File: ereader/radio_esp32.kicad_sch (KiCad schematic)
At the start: 32 parts, among them U25 TXU0102DCUR, U3 ESP32-C6-WROOM-1-N8, U4 TPS22964CYZPT, U5 TXU0304PWR, U6 TPS389001DSET, U7 SN74LVC1G97DBVR, U8 SN74LVC1G97DBVR

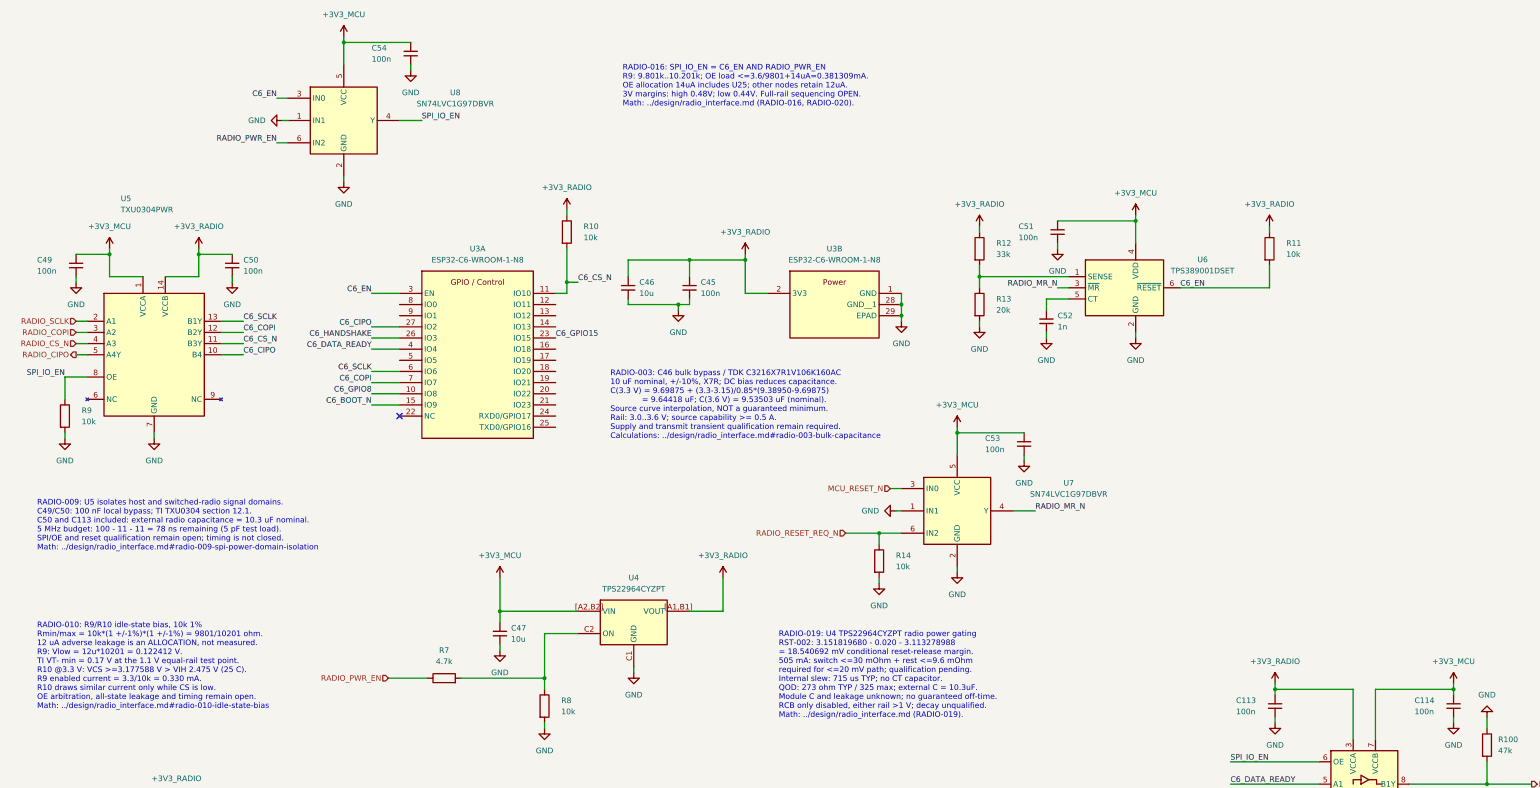
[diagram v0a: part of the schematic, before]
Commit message: WIP: integrate orientation sensor and refresh schematic review exports
Add LIS2DW12 host wiring and sourced passives, revise held-supply discharge calculations, document camera and capacitance screens, and refresh standard capacitor caches. Include reviewed 14-page PDF and reconciled native BOM. ERC remains 111 errors and 11 warnings; electrical design is incomplete. Refs #21.
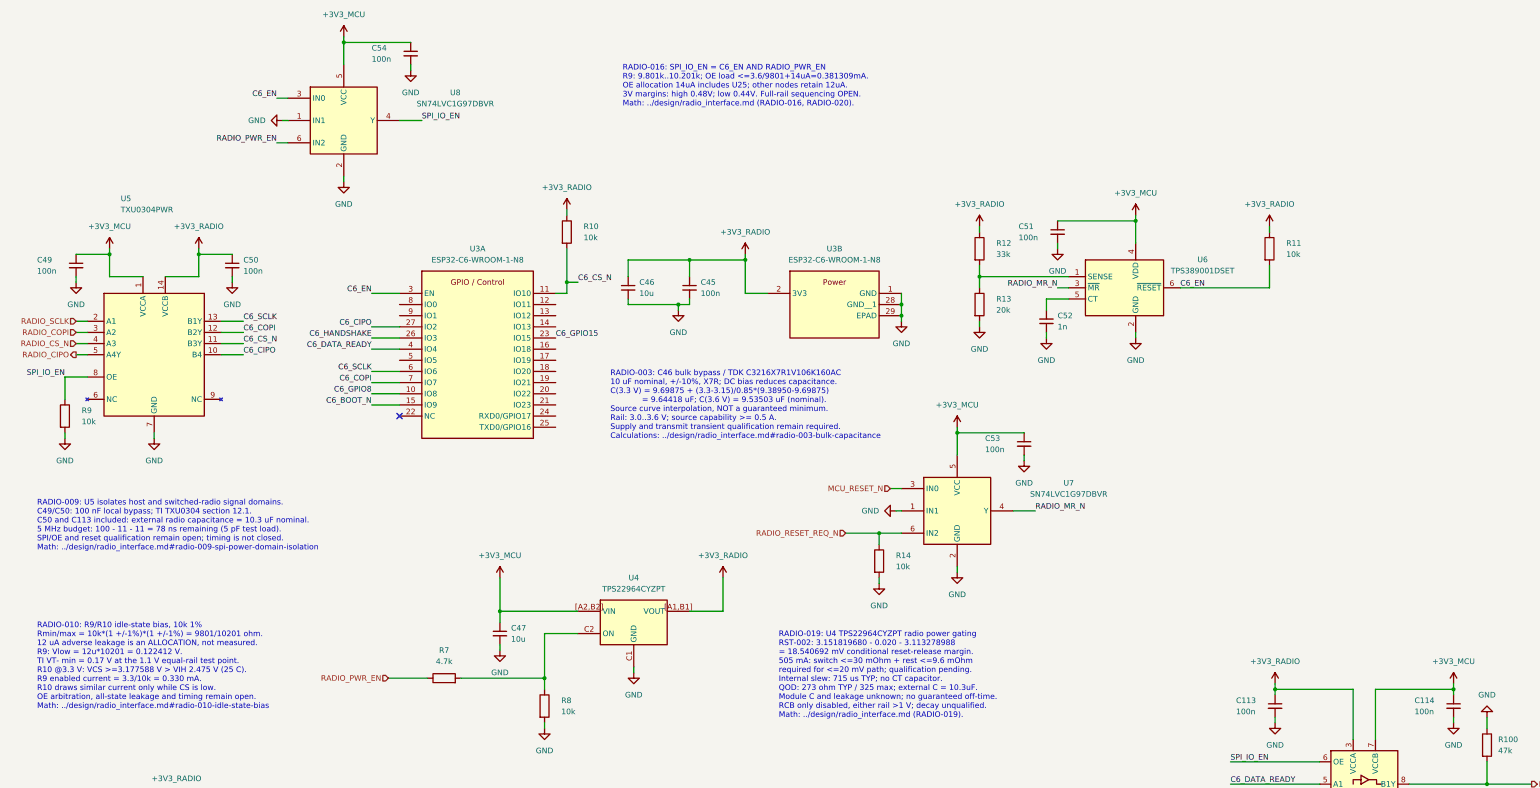
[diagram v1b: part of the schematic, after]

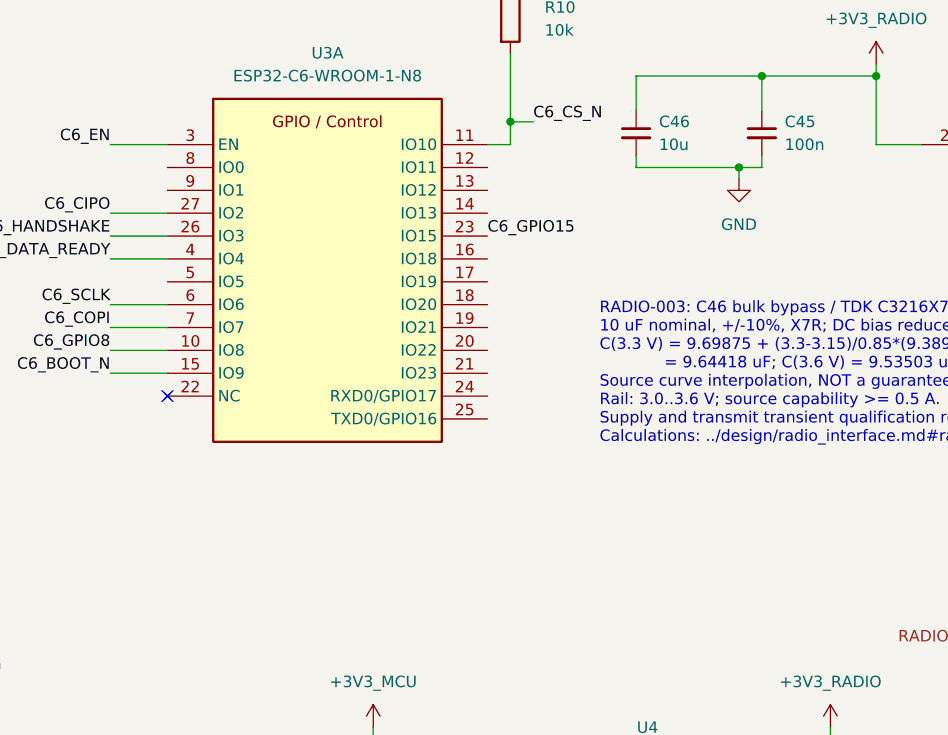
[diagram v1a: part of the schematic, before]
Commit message: Document and mark unused radio GPIOs while preserving recovery pins
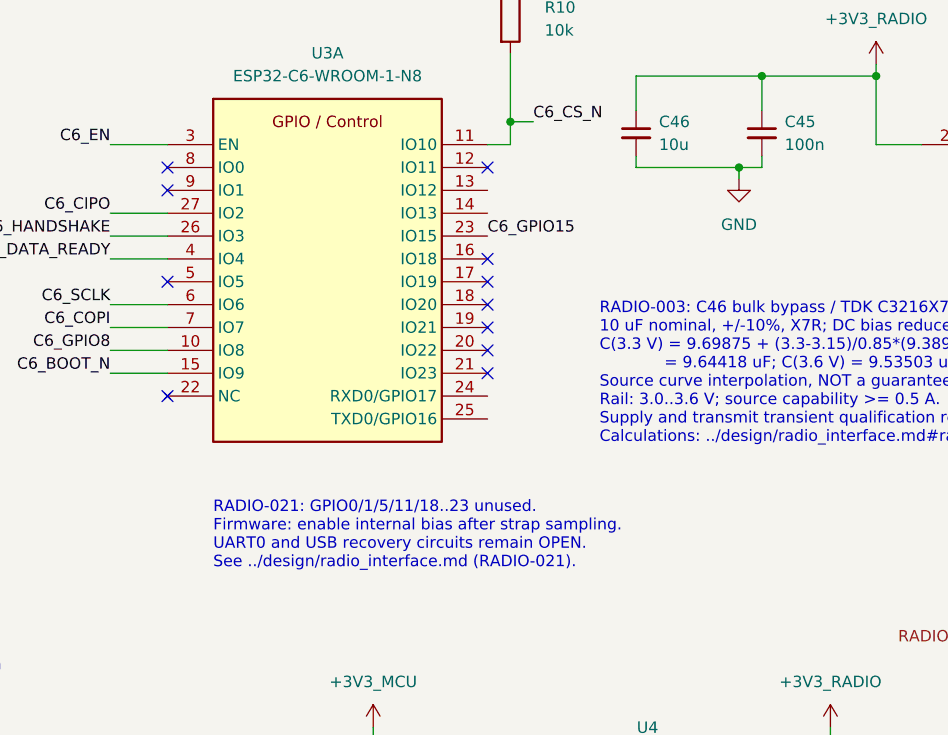
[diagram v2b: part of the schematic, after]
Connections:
- no-connect marks 1 -> 11
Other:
- note added: "RADIO-021: GPIO0/1/5/11/18..23 unused. Firmware: enable internal bias after strap sampling. UART0 and USB recovery circuits remain OPEN. See ../design/radio_interface.md (RADIO-021)."
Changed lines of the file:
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@@
+		)
+	)
+	(text "RADIO-021: GPIO0/1/5/11/18..23 unused.\nFirmware: enable internal bias after strap sampling.\nUART0 and USB recovery circuits remain OPEN.\nSee ../design/radio_interface.md (RADIO-021)."
+		(exclude_from_sim no)
+		(at 106.68 120.904 0)
+		(effects
+			(font
+				(size 1.27 1.27)
+			)
+			(justify left)
 		)
 	)
@@
 	)
 	(no_connect
+		(at 137.16 100.33)
+	)
+	(no_connect
+		(at 137.16 102.87)
+	)
+	(no_connect
+		(at 101.6 82.55)
+	)
+	(no_connect
+		(at 137.16 90.17)
+	)
+	(no_connect
+		(at 101.6 80.01)
+	)
+	(no_connect
+		(at 137.16 80.01)
+	)
+	(no_connect
+		(at 137.16 95.25)
+	)
+	(no_connect
 		(at 101.6 105.41)
 	)
+	(no_connect
+		(at 137.16 92.71)
+	)
+	(no_connect
+		(at 101.6 92.71)
+	)
+	(no_connect
+		(at 137.16 97.79)
+	)
 	(wire

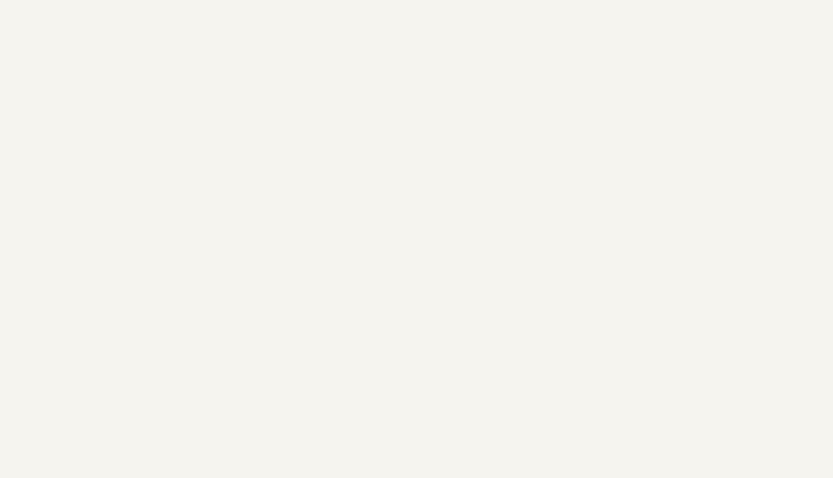
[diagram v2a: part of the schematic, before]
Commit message: Checkpoint native UART translator placement and refresh schematic PDF
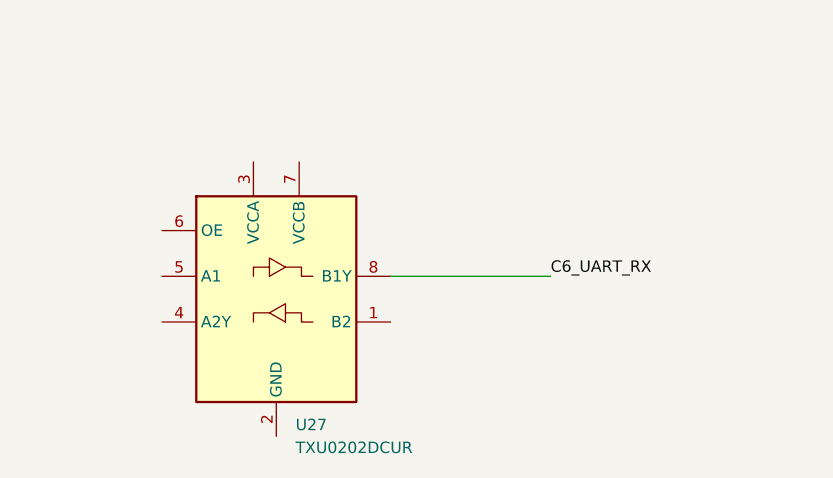
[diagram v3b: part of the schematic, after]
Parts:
- added U27: TXU0202DCUR, symbol Power_Devices:TXU0202DCUR
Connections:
- new net C6_UART_RX: U27.8 (B1Y)
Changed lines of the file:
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@@
 	(wire
 		(pts
+			(xy 160.02 328.93) (xy 177.8 328.93)
+		)
+		(stroke
+			(width 0)
+			(type default)
+		)
+	)
+	(wire
+		(pts
 			(xy 139.7 74.93) (xy 139.7 77.47)
 		)
@@
 		)
 	)
+	(label "C6_UART_RX"
+		(at 177.8 328.93 0)
+		(effects
+			(font
+				(size 1.27 1.27)
+			)
+			(justify left bottom)
+		)
+	)
 	(label "C6_HANDSHAKE"
 		(at 95.25 87.63 180)
@@
 					(unit 1)
 				)
+			)
+		)
+	)
+	(symbol
+		(lib_id "Power_Devices:TXU0202DCUR")
+		(at 147.32 331.47 0)
+		(unit 1)
+		(body_style 1)
+		(exclude_from_sim no)
+		(in_bom yes)
+		(on_board yes)
+		(in_pos_files yes)
+		(dnp no)
+		(fields_autoplaced yes)
+		(property "Reference" "U27"
+			(at 149.4633 345.44 0)
+			(show_name no)
+			(do_not_autoplace no)
+			(effects
+				(font
+					(size 1.27 1.27)
+				)
+				(justify left)
+			)
+		)
+		(property "Value" "TXU0202DCUR"
+			(at 149.4633 347.98 0)
+			(show_name no)
+			(do_not_autoplace no)
+			(effects
+				(font
+					(size 1.27 1.27)
+				)
+				(justify left)
+			)
+		)
+		(property "Footprint" ""
+			(at 147.32 345.44 0)
+			(hide yes)
+			(show_name no)
+			(do_not_autoplace no)
+			(effects
+				(font
+					(size 1.27 1.27)
+				)
+			)
+		)
+		(property "Datasheet" "https://www.ti.com/lit/ds/symlink/txu0202.pdf"
+			(at 147.32 332.232 0)
+			(hide yes)
+			(show_name no)
+			(do_not_autoplace no)
+			(effects
+				(font
+					(size 1.27 1.27)
+				)
+			)
+		)
+		(property "Description" "TI TXU0202DCUR; one A-to-B and one B-to-A fixed-direction translator, active-high OE, 1.1..5.5 V, VSSOP-8 DCU. Pins 1=B2, 2=GND, 3=VCCA, 4=A2Y, 5=A1, 6=OE, 7=VCCB, 8=B1Y. SCES942A Table 6-1."
+			(at 147.32 331.47 0)
+			(hide yes)
+			(show_name no)
+			(do_not_autoplace no)
+			(effects
+				(font
+					(size 1.27 1.27)
+				)
+			)
+		)
+		(property "Manufacturer_Name" "Texas Instruments"
+			(at 147.32 331.47 0)
+			(hide yes)
+			(show_name no)
+			(do_not_autoplace no)
+			(effects
+				(font
+					(size 1.27 1.27)
+				)
+			)
+		)
+		(property "Manufacturer_Part_Number" "TXU0202DCUR"
+			(at 147.32 331.47 0)
+			(hide yes)
+			(show_name no)
+			(do_not_autoplace no)
+			(effects
+				(font
+					(size 1.27 1.27)
+				)
+			)
+		)
+		(property "DigiKey_Part_Number" "296-TXU0202DCURCT-ND"
+			(at 147.32 331.47 0)
+			(hide yes)
+			(show_name no)
+			(do_not_autoplace no)
+			(effects
+				(font
+					(size 1.27 1.27)
+				)
+			)
+		)
+		(property "DigiKey_URL" "https://www.digikey.com/en/products/detail/texas-instruments/TXU0202DCUR/16677096"
+			(at 147.32 331.47 0)
+			(hide yes)
+			(show_name no)
+			(do_not_autoplace no)
+			(effects
+				(font
+					(size 1.27 1.27)
+				)
+			)
+		)
+		(pin "2"
+		)
+		(pin "4"
+		)
+		(pin "6"
+		)
+		(pin "3"
+		)
+		(pin "1"
+		)
+		(pin "5"
+		)
+		(pin "8"
+		)
+		(pin "7"
+		)
+		(instances
+			(project "ereader_rev1"
+				(path "/0586cc51-9c57-495b-a0c9-c29ba0d48166/9b84c337-6879-4714-899e-3993bcc30b88"
+					(reference "U27")
+					(unit 1)
+				)

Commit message: Wire radio service UART and ground; refresh schematic PDF
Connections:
- net C6_UART_RX: now also U3.24 (RXD0/GPIO17)
- net GND: now also U27.2 (GND)
- net C6_UART_TX: now reaches U3.25 (TXD0/GPIO16)
- net C6_UART_TX: now also U27.1 (B2)
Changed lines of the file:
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@@
 	(wire
 		(pts
+			(xy 137.16 107.95) (xy 139.7 107.95)
+		)
+		(stroke
+			(width 0)
+			(type default)
+		)
+	)
+	(wire
+		(pts
 			(xy 233.68 62.23) (xy 233.68 63.5)
 		)
@@
 	(wire
 		(pts
+			(xy 142.24 105.41) (xy 142.24 113.03)
+		)
+		(stroke
+			(width 0)
+			(type default)
+		)
+	)
+	(wire
+		(pts
 			(xy 124.46 158.75) (xy 124.46 157.48)
 		)
@@
 	(wire
 		(pts
+			(xy 147.32 346.71) (xy 147.32 351.79)
+		)
+		(stroke
+			(width 0)
+			(type default)
+		)
+	)
+	(wire
+		(pts
 			(xy 243.84 109.22) (xy 228.6 109.22)
 		)
@@
 	(wire
 		(pts
+			(xy 137.16 105.41) (xy 142.24 105.41)
+		)
+		(stroke
+			(width 0)
+			(type default)
+		)
+	)
+	(wire
+		(pts
 			(xy 95.25 100.33) (xy 101.6 100.33)
 		)
@@
 	(wire
 		(pts
+			(xy 160.02 334.01) (xy 177.8 334.01)
+		)
+		(stroke
+			(width 0)
+			(type default)
+		)
+	)
+	(wire
+		(pts
 			(xy 60.96 91.44) (xy 66.04 91.44)
 		)
@@
 	(wire
 		(pts
+			(xy 139.7 107.95) (xy 139.7 115.57)
+		)
+		(stroke
+			(width 0)
+			(type default)
+		)
+	)
+	(wire
+		(pts
 			(xy 25.4 193.04) (xy 25.4 199.39)
 		)
@@
 		)
 	)
+	(label "C6_UART_TX"
+		(at 177.8 334.01 0)
+		(effects
+			(font
+				(size 1.27 1.27)
+			)
+			(justify left bottom)
+		)
+	)
 	(label "C6_DATA_READY"
 		(at 290.83 189.23 0)
@@
 		)
 	)
+	(label "C6_UART_RX"
+		(at 142.24 113.03 0)
+		(effects
+			(font
+				(size 1.27 1.27)
+			)
+			(justify left bottom)
+		)
+	)
 	(label "C6_COPI"
 		(at 66.04 86.36 0)
@@
 		)
 	)
+	(label "C6_UART_TX"
+		(at 139.7 115.57 0)
+		(effects
+			(font
+				(size 1.27 1.27)
+			)
+			(justify left bottom)
+		)
+	)
 	(label "C6_SCLK"
 		(at 66.04 83.82 0)
@@
 					(unit 1)
 				)
+			)
+		)
+	)
+	(symbol
+		(lib_id "power:GND")
+		(at 147.32 351.79 0)
+		(unit 1)
+		(body_style 1)
+		(exclude_from_sim no)
+		(in_bom yes)
+		(on_board yes)
+		(in_pos_files yes)
+		(dnp no)
+		(fields_autoplaced yes)
+		(property "Reference" "#PWR0241"
+			(at 147.32 358.14 0)
+			(hide yes)
+			(show_name no)
+			(do_not_autoplace no)
+			(effects
+				(font
+					(size 1.27 1.27)
+				)
+			)
+		)
+		(property "Value" "GND"
+			(at 147.32 356.87 0)
+			(show_name no)
+			(do_not_autoplace no)
+			(effects
+				(font
+					(size 1.27 1.27)
+				)
+			)
+		)
+		(property "Footprint" ""
+			(at 147.32 351.79 0)
+			(hide yes)
+			(show_name no)
+			(do_not_autoplace no)
+			(effects
+				(font
+					(size 1.27 1.27)
+				)
+			)
+		)
+		(property "Datasheet" ""
+			(at 147.32 351.79 0)
+			(hide yes)
+			(show_name no)
+			(do_not_autoplace no)
+			(effects
+				(font
+					(size 1.27 1.27)
+				)
+			)
+		)
+		(property "Description" "Power symbol creates a global label with name \"GND\" , ground"
+			(at 147.32 351.79 0)
+			(hide yes)
+			(show_name no)
+			(do_not_autoplace no)
+			(effects
+				(font
+					(size 1.27 1.27)
+				)
+			)
+		)
+		(pin "1"
+		)
+		(instances
+			(project "ereader_rev1"
+				(path "/0586cc51-9c57-495b-a0c9-c29ba0d48166/9b84c337-6879-4714-899e-3993bcc30b88"
+					(reference "#PWR0241")
+					(unit 1)
+				)

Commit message: Route isolated UART supply domains and refresh schematic PDF
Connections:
- net +3V3_RADIO: now also U27.7 (VCCB)
- net SERVICE_VIO: now reaches U27.3 (VCCA)
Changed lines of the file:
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@@
 	(wire
 		(pts
+			(xy 124.46 306.07) (xy 144.78 306.07)
+		)
+		(stroke
+			(width 0)
+			(type default)
+		)
+	)
+	(wire
+		(pts
 			(xy 185.42 77.47) (xy 180.34 77.47)
 		)
@@
 	(wire
 		(pts
+			(xy 149.86 306.07) (xy 170.18 306.07)
+		)
+		(stroke
+			(width 0)
+			(type default)
+		)
+	)
+	(wire
+		(pts
 			(xy 299.72 62.23) (xy 299.72 63.5)
 		)
@@
 	(wire
 		(pts
+			(xy 149.86 316.23) (xy 149.86 306.07)
+		)
+		(stroke
+			(width 0)
+			(type default)
+		)
+	)
+	(wire
+		(pts
 			(xy 60.96 86.36) (xy 66.04 86.36)
 		)
@@
 	(wire
 		(pts
+			(xy 144.78 316.23) (xy 144.78 306.07)
+		)
+		(stroke
+			(width 0)
+			(type default)
+		)
+	)
+	(wire
+		(pts
 			(xy 73.66 43.18) (xy 76.2 43.18)
 		)
@@
 		)
 	)
+	(label "SERVICE_VIO"
+		(at 124.46 306.07 0)
+		(effects
+			(font
+				(size 1.27 1.27)
+			)
+			(justify left bottom)
+		)
+	)
 	(label "C6_EN"
 		(at 73.66 33.02 180)
@@
 					(unit 1)
 				)
+			)
+		)
+	)
+	(symbol
+		(lib_id "power:+3V3")
+		(at 170.18 306.07 0)
+		(unit 1)
+		(body_style 1)
+		(exclude_from_sim no)
+		(in_bom yes)
+		(on_board yes)
+		(in_pos_files yes)
+		(dnp no)
+		(fields_autoplaced yes)
+		(property "Reference" "#PWR0242"
+			(at 170.18 309.88 0)
+			(hide yes)
+			(show_name no)
+			(do_not_autoplace no)
+			(effects
+				(font
+					(size 1.27 1.27)
+				)
+			)
+		)
+		(property "Value" "+3V3_RADIO"
+			(at 170.18 300.99 0)
+			(show_name no)
+			(do_not_autoplace no)
+			(effects
+				(font
+					(size 1.27 1.27)
+				)
+			)
+		)
+		(property "Footprint" ""
+			(at 170.18 306.07 0)
+			(hide yes)
+			(show_name no)
+			(do_not_autoplace no)
+			(effects
+				(font
+					(size 1.27 1.27)
+				)
+			)
+		)
+		(property "Datasheet" ""
+			(at 170.18 306.07 0)
+			(hide yes)
+			(show_name no)
+			(do_not_autoplace no)
+			(effects
+				(font
+					(size 1.27 1.27)
+				)
+			)
+		)
+		(property "Description" "Power symbol creates a global label with name \"+3V3\""
+			(at 170.18 306.07 0)
+			(hide yes)
+			(show_name no)
+			(do_not_autoplace no)
+			(effects
+				(font
+					(size 1.27 1.27)
+				)
+			)
+		)
+		(pin "1"
+		)
+		(instances
+			(project "ereader_rev1"
+				(path "/0586cc51-9c57-495b-a0c9-c29ba0d48166/9b84c337-6879-4714-899e-3993bcc30b88"
+					(reference "#PWR0242")
+					(unit 1)
+				)

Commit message: Add service UART supply bypass capacitors and refresh PDF
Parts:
- added C116, C119: 100n, symbol Device:C_Small
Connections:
- net +3V3_RADIO: now also C119.1
- net GND: now also C116.2, C119.2
- net SERVICE_VIO: now also C116.1

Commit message: Add service UART enable pull-down and refresh schematic PDF
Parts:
- added R104: 47k, symbol Device:R
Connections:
- net GND: now also R104.2
- net SERVICE_UART_OE: now reaches U27.6 (OE)
- net SERVICE_UART_OE: now also R104.1
